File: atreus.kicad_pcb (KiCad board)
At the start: 2 copper layers, 232 x 90 mm, 85 parts

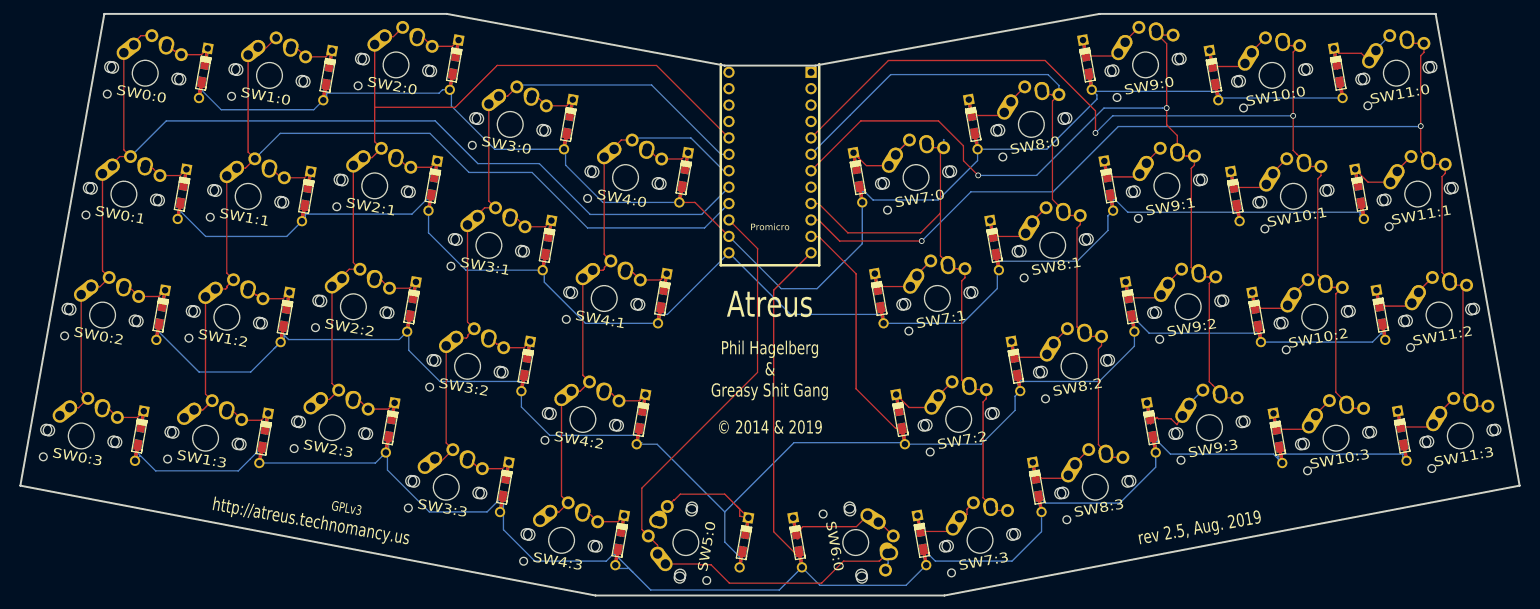
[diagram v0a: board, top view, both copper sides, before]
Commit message: lowered promicro and manual routing again.
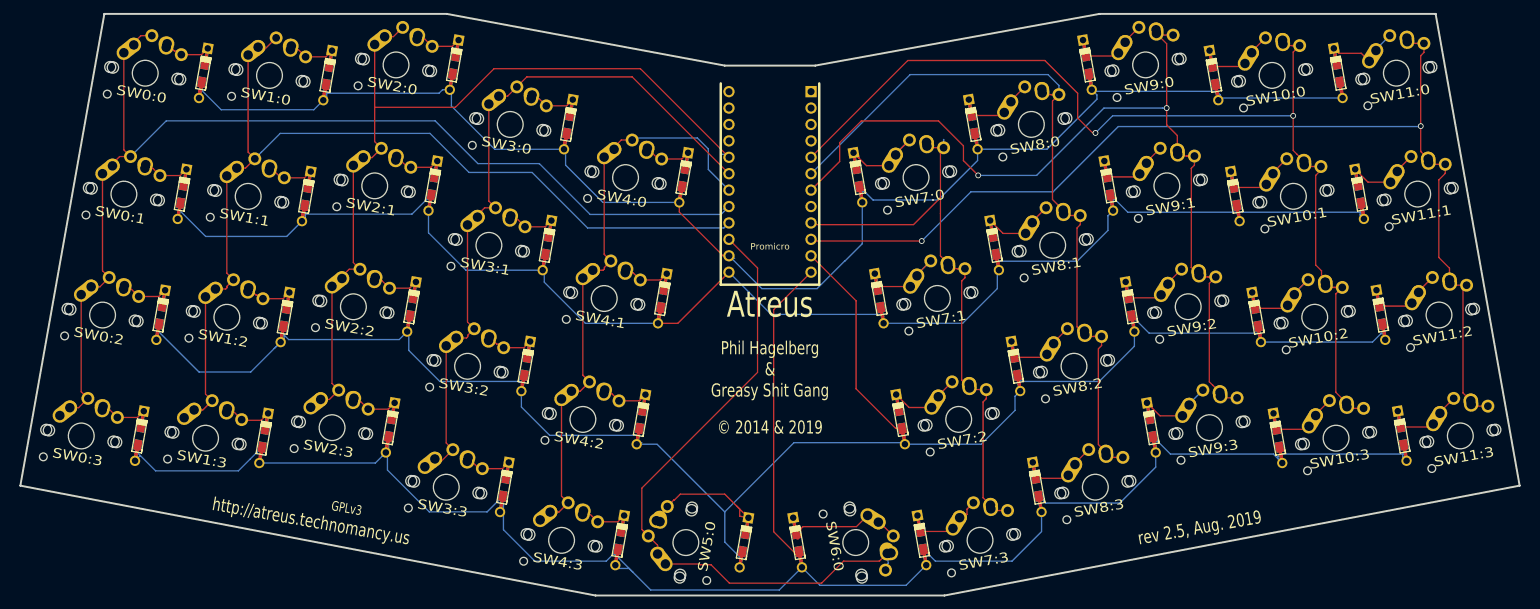
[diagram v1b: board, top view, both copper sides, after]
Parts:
- moved Promicro 3.00 mm to (134.0, 48.0)
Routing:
- net N-row-2: track 332.1 -> 328.5 mm
- net N-diode-39: track 18.9 -> 15.6 mm
- net N-col-4: track 91.9 -> 95.0 mm
- net N-row-3: track 337.9 -> 334.9 mm
- net N-col-5: track 106.7 -> 103.7 mm
- net N-col-8: track 140.7 -> 143.7 mm
- net N-row-1: track 268.8 -> 265.9 mm
- net N-col-3: track 110.0 -> 112.7 mm
- net N-row-0: track 267.8 -> 269.9 mm
- net N-col-2: track 135.2 -> 137.2 mm
- net N-col-6: track 96.6 -> 94.6 mm
- net N-diode-23: track 18.0 -> 16.1 mm
- net N-col-9: track 162.8 -> 164.5 mm
- net N-col-1: track 157.2 -> 156.0 mm
- net N-col-7: track 119.0 -> 120.3 mm
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
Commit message: promicro, trace, and revision.
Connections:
- Promicro pad B1: N-col-1 -> N-col-3
- Promicro pad B2: N-row-0 -> N-row-1
- Promicro pad B3: N-col-5 -> N-col-4
- Promicro pad B6: N-row-1 -> N-col-5
- Promicro pad C6: (no net) -> N-col-8
- Promicro pad D0: N-col-7 -> N-col-10
- Promicro pad D1: N-col-9 -> (no net)
- Promicro pad D4: N-col-8 -> N-col-9
- Promicro pad D7: N-col-6 -> N-col-7
- Promicro pad E6: N-col-10 -> N-col-6
- Promicro pad F4: N-col-2 -> N-row-0
- Promicro pad F5: N-col-3 -> N-col-0
- Promicro pad F6: N-col-4 -> N-col-1
- Promicro pad F7: N-col-0 -> N-col-2
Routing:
- net N-row-2: track 328.5 -> 268.0 mm
- net N-row-3: track 334.9 -> 280.0 mm
- net N-row-1: track 265.9 -> 225.7 mm
- net N-row-0: track 269.9 -> 237.4 mm
- net N-col-5: track 103.7 -> 92.2 mm
- net N-col-9: track 164.5 -> 153.6 mm, vias 2 -> 0
- net N-col-8: track 143.7 -> 133.1 mm, vias 2 -> 0
- net N-diode-21: track 21.4 -> 11.6 mm
- net N-diode-20: track 26.7 -> 17.0 mm
- net N-diode-24: track 28.2 -> 19.1 mm
- net N-diode-28: track 20.7 -> 11.6 mm
- net N-diode-29: track 18.4 -> 11.6 mm
- net N-col-7: track 120.3 -> 113.5 mm
- net N-diode-26: track 17.9 -> 11.6 mm
- net N-diode-38: track 17.7 -> 11.6 mm
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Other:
- board text added: "rev 2.6, Sept. 2019"
- board text removed: "rev 2.5, Aug. 2019"

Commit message: new branch, only chocs.
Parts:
- moved D0:0 8.72 mm to (46.1, 39.9)
- moved SW0:0 8.72 mm to (37.1, 39.9)
- moved D11:0 8.69 mm to (221.8, 39.9)
- moved SW11:0 8.69 mm to (230.8, 39.9)
- moved D0:1 7.74 mm to (43.0, 57.6)
- moved SW0:1 7.74 mm to (34.0, 57.6)
- moved D11:1 7.71 mm to (224.9, 57.6)
- moved SW11:1 7.71 mm to (233.9, 57.6)
- moved D0:2 6.75 mm to (39.9, 75.4)
- moved SW0:2 6.75 mm to (30.9, 75.4)
- moved D11:2 6.74 mm to (228.1, 75.3)
- moved SW11:2 6.74 mm to (237.1, 75.3)
- moved SW0:3 5.77 mm to (27.7, 93.1)
- moved D0:3 5.77 mm to (36.7, 93.1)
- moved D11:3 5.77 mm to (231.2, 93.0)
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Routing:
- net N-row-2: track 268.0 -> 277.5 mm
- net N-col-3: track 111.0 -> 101.7 mm
- net N-col-1: track 153.3 -> 144.6 mm
- net N-col-2: track 132.9 -> 125.4 mm
- net N-col-4: track 90.0 -> 83.6 mm
- net N-col-7: track 113.5 -> 107.4 mm
- net N-col-0: track 174.6 -> 168.9 mm
- net N-row-1: track 225.7 -> 231.2 mm
- net N-col-8: track 133.1 -> 128.0 mm
- net N-col-9: track 153.6 -> 148.9 mm
- net N-col-5: track 92.2 -> 96.5 mm
- net N-col-10: track 175.6 -> 171.5 mm
- net N-row-0: track 237.4 -> 241.2 mm
- net N-diode-20: track 17.0 -> 13.4 mm
- net N-diode-2: track 7.39 -> 4.26 mm
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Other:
- board size 232 x 90 mm -> 234 x 90 mm
- board text added: "rev 2.6-choc, Sept. 2019"
- board text removed: "rev 2.6, Sept. 2019"

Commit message: case for choc.
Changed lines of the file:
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@@
    (net 2 N-row-1)))
 (module Keebio-Parts:MX-Alps-Choc-1U-NoLED (layer Front)
-  (at 30.87048249320629 75.35086260162737 -10)
+  (at 30.8704824932063 75.35086260162736 -10)
   (fp_text
    reference
@@
    (net 5 N-col-0)))
 (module DIODE (layer Front)
-  (at 39.87048249320629 75.35086260162737 80)
+  (at 39.870482493206296 75.35086260162736 80)
   (attr smd)
   (fp_text
@@
    (net 2 N-row-1)))
 (module Keebio-Parts:MX-Alps-Choc-1U-NoLED (layer Front)
-  (at 50.333503824095345 68.62845226951004 -10)
+  (at 50.333503824095345 68.62845226951003 -10)
   (fp_text
    reference
@@
    (net 6 N-col-1)))
 (module DIODE (layer Front)
-  (at 59.333503824095345 68.62845226951004 80)
+  (at 59.333503824095345 68.62845226951003 80)
   (attr smd)
   (fp_text
@@
    (net 2 N-row-1)))
 (module Keebio-Parts:MX-Alps-Choc-1U-NoLED (layer Front)
-  (at 85.6129347548679 75.86459441853174 -10)
+  (at 85.61293475486791 75.86459441853172 -10)
   (fp_text
    reference
@@
    (net 8 N-col-3)))
 (module DIODE (layer Front)
-  (at 94.6129347548679 75.86459441853174 80)
+  (at 94.61293475486791 75.86459441853172 80)
   (attr smd)
   (fp_text

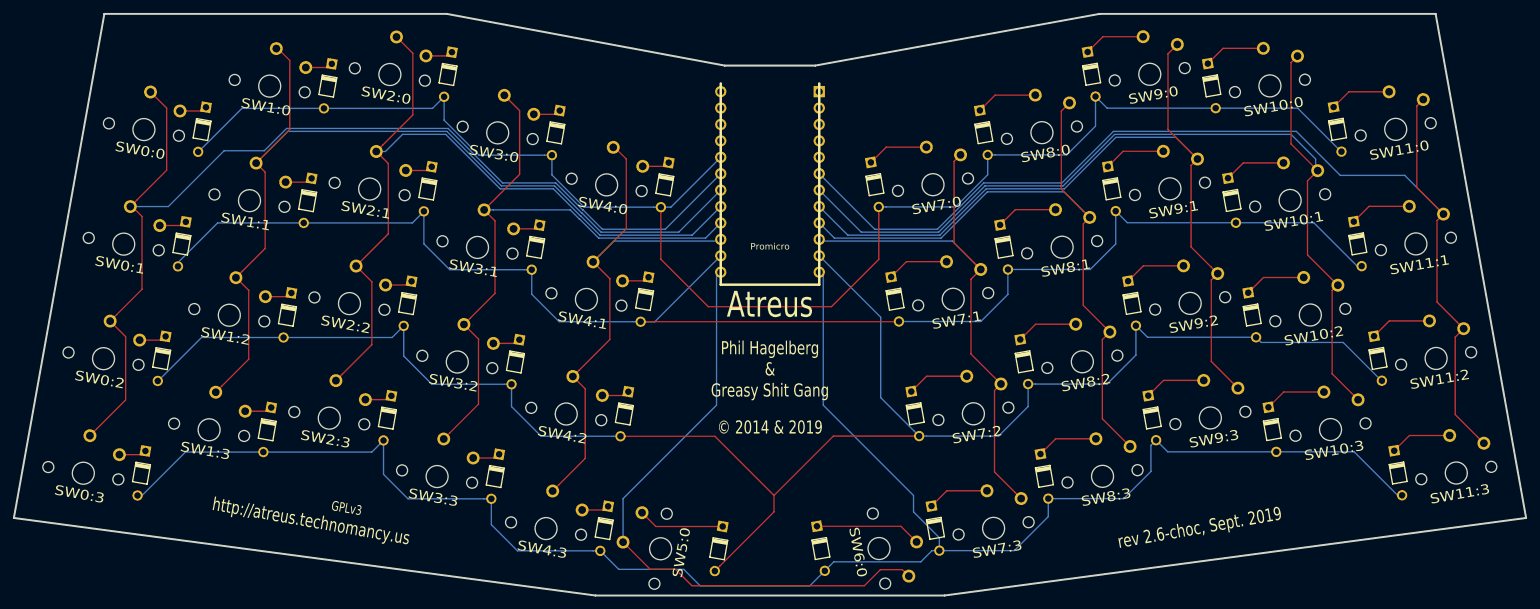
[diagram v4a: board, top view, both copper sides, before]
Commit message: changed the footprint
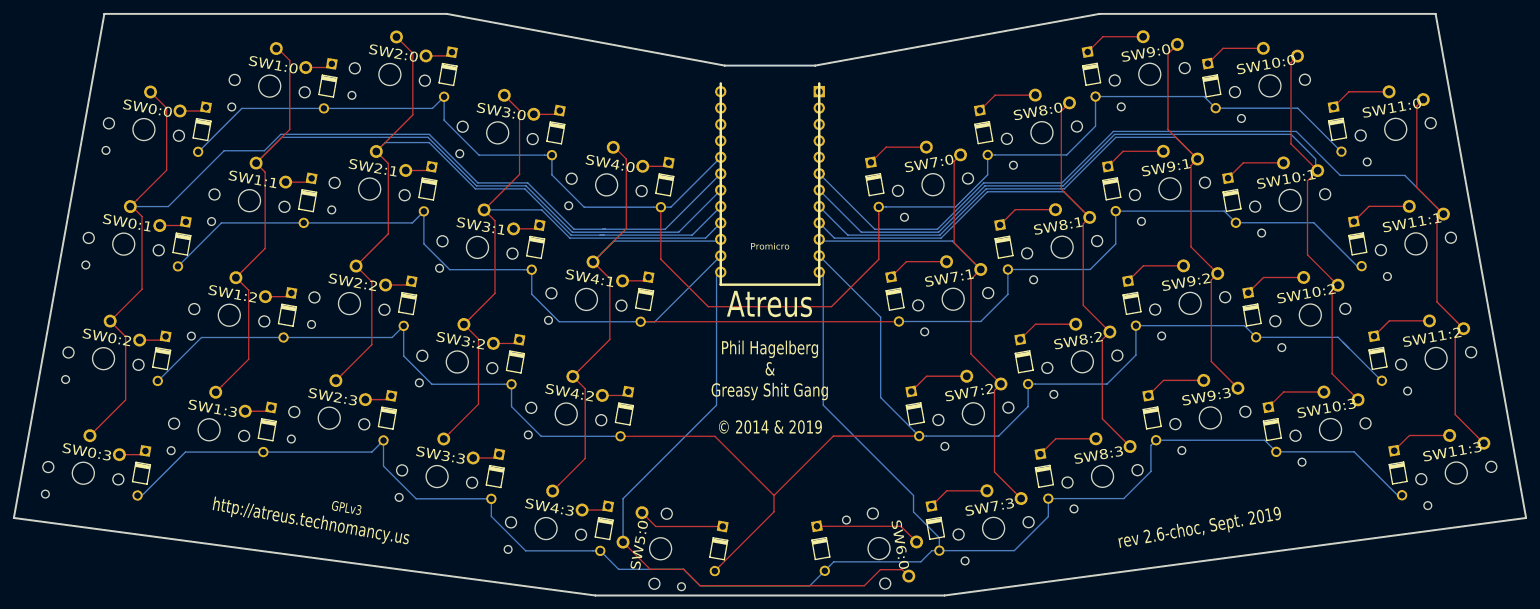
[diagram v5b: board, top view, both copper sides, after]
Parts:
- turned SW3:2 to 170 degrees
- turned SW0:2 to 170 degrees
- turned SW0:0 to 170 degrees
- turned SW0:1 to 170 degrees
- turned SW0:3 to 170 degrees
- turned SW10:0 to 190 degrees
- turned SW10:1 to 190 degrees
- turned SW10:2 to 190 degrees
- turned SW10:3 to 190 degrees
- turned SW11:0 to 190 degrees
- turned SW11:1 to 190 degrees
- turned SW11:2 to 190 degrees
- turned SW11:3 to 190 degrees
- turned SW1:0 to 170 degrees
- turned SW1:1 to 170 degrees
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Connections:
- SW0:0 pad 1: N-diode-0 -> N-col-0
- SW0:0 pad 2: N-col-0 -> N-diode-0
- SW0:1 pad 1: N-diode-1 -> N-col-0
- SW0:1 pad 2: N-col-0 -> N-diode-1
- SW0:2 pad 1: N-diode-2 -> N-col-0
- SW0:2 pad 2: N-col-0 -> N-diode-2
- SW0:3 pad 1: N-diode-3 -> N-col-0
- SW0:3 pad 2: N-col-0 -> N-diode-3
- SW10:0 pad 1: N-col-9 -> N-diode-40
- SW10:0 pad 2: N-diode-40 -> N-col-9
- SW10:1 pad 1: N-col-9 -> N-diode-41
- SW10:1 pad 2: N-diode-41 -> N-col-9
- SW10:2 pad 1: N-col-9 -> N-diode-21
- SW10:2 pad 2: N-diode-21 -> N-col-9
- SW10:3 pad 1: N-col-9 -> N-diode-22
- SW10:3 pad 2: N-diode-22 -> N-col-9
- SW11:0 pad 1: N-col-10 -> N-diode-23
- SW11:0 pad 2: N-diode-23 -> N-col-10
- SW11:1 pad 1: N-col-10 -> N-diode-25
- SW11:1 pad 2: N-diode-25 -> N-col-10
- SW11:2 pad 1: N-col-10 -> N-diode-26
- SW11:2 pad 2: N-diode-26 -> N-col-10
- SW11:3 pad 1: N-col-10 -> N-diode-27
- SW11:3 pad 2: N-diode-27 -> N-col-10
- SW1:0 pad 1: N-diode-4 -> N-col-1
- SW1:0 pad 2: N-col-1 -> N-diode-4
- SW1:1 pad 1: N-diode-5 -> N-col-1
- SW1:1 pad 2: N-col-1 -> N-diode-5
- SW1:2 pad 1: N-diode-6 -> N-col-1
- SW1:2 pad 2: N-col-1 -> N-diode-6
- SW1:3 pad 1: N-diode-7 -> N-col-1
- SW1:3 pad 2: N-col-1 -> N-diode-7
- SW2:0 pad 1: N-diode-8 -> N-col-2
- SW2:0 pad 2: N-col-2 -> N-diode-8
- SW2:1 pad 1: N-diode-9 -> N-col-2
- SW2:1 pad 2: N-col-2 -> N-diode-9
- SW2:2 pad 1: N-diode-10 -> N-col-2
- SW2:2 pad 2: N-col-2 -> N-diode-10
- SW2:3 pad 1: N-diode-11 -> N-col-2
- SW2:3 pad 2: N-col-2 -> N-diode-11
- SW3:0 pad 1: N-diode-12 -> N-col-3
- SW3:0 pad 2: N-col-3 -> N-diode-12
- SW3:1 pad 1: N-diode-13 -> N-col-3
- SW3:1 pad 2: N-col-3 -> N-diode-13
- SW3:2 pad 1: N-diode-14 -> N-col-3
- SW3:2 pad 2: N-col-3 -> N-diode-14
- SW3:3 pad 1: N-diode-15 -> N-col-3
- SW3:3 pad 2: N-col-3 -> N-diode-15
- SW4:0 pad 1: N-diode-16 -> N-col-4
- SW4:0 pad 2: N-col-4 -> N-diode-16
- SW4:1 pad 1: N-diode-17 -> N-col-4
- SW4:1 pad 2: N-col-4 -> N-diode-17
- SW4:2 pad 1: N-diode-18 -> N-col-4
- SW4:2 pad 2: N-col-4 -> N-diode-18
- SW4:3 pad 1: N-diode-19 -> N-col-4
- SW4:3 pad 2: N-col-4 -> N-diode-19
- SW5:0 pad 1: N-diode-20 -> N-col-5
- SW5:0 pad 2: N-col-5 -> N-diode-20
- SW6:0 pad 1: N-col-5 -> N-diode-24
- SW6:0 pad 2: N-diode-24 -> N-col-5
- SW7:0 pad 1: N-col-6 -> N-diode-28
- SW7:0 pad 2: N-diode-28 -> N-col-6
- SW7:1 pad 1: N-col-6 -> N-diode-29
- SW7:1 pad 2: N-diode-29 -> N-col-6
- SW7:2 pad 1: N-col-6 -> N-diode-30
- SW7:2 pad 2: N-diode-30 -> N-col-6
- SW7:3 pad 1: N-col-6 -> N-diode-31
- SW7:3 pad 2: N-diode-31 -> N-col-6
- SW8:0 pad 1: N-col-7 -> N-diode-32
- SW8:0 pad 2: N-diode-32 -> N-col-7
- SW8:1 pad 1: N-col-7 -> N-diode-33
- SW8:1 pad 2: N-diode-33 -> N-col-7
- SW8:2 pad 1: N-col-7 -> N-diode-34
- SW8:2 pad 2: N-diode-34 -> N-col-7
- SW8:3 pad 1: N-col-7 -> N-diode-35
- SW8:3 pad 2: N-diode-35 -> N-col-7
- SW9:0 pad 1: N-col-8 -> N-diode-36
- SW9:0 pad 2: N-diode-36 -> N-col-8
- SW9:1 pad 1: N-col-8 -> N-diode-37
- SW9:1 pad 2: N-diode-37 -> N-col-8
- SW9:2 pad 1: N-col-8 -> N-diode-38
- SW9:2 pad 2: N-diode-38 -> N-col-8
- SW9:3 pad 1: N-col-8 -> N-diode-39
- SW9:3 pad 2: N-diode-39 -> N-col-8
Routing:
- net N-row-3: track 281.0 -> 279.5 mm
- net N-row-2: track 277.5 -> 278.6 mm
- net N-col-1: track 144.6 -> 143.8 mm
